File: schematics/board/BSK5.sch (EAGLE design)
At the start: 26 parts

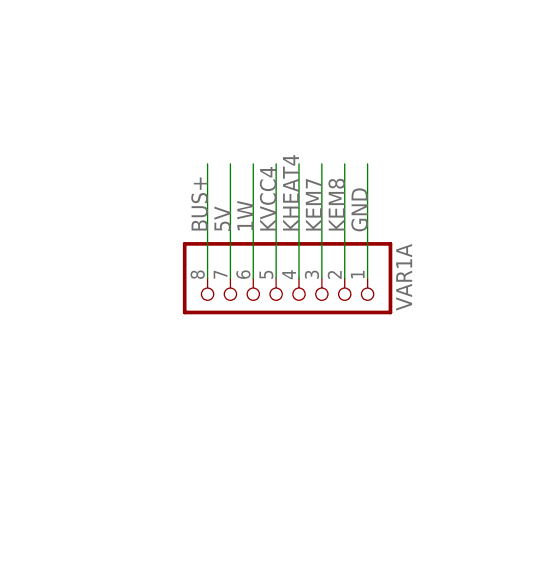
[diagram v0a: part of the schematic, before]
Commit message: Подписаны разъемы на платах
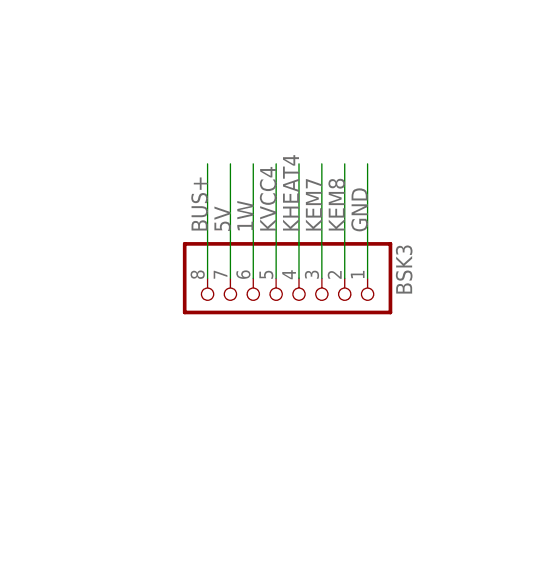
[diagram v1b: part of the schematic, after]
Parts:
- renumbered VAR1A to BSK3
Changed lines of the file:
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@@
 <part name="U$11" library="CanCubeSat" deviceset="KCONNECT" device=""/>
 <part name="U$12" library="CanCubeSat" deviceset="KCONNECT" device=""/>
-<part name="VAR1A" library="pinheadCS" deviceset="PINHD-1X8" device=""/>
+<part name="BSK3" library="pinheadCS" deviceset="PINHD-1X8" device=""/>
 <part name="LED2" library="led" library_urn="urn:adsk.eagle:library:259" deviceset="LED" device="CHIPLED_0603" package3d_urn="urn:adsk.eagle:package:15822/2"/>
 <part name="R81" library="resistor" library_urn="urn:adsk.eagle:library:348" deviceset="R-US_" device="R0603" package3d_urn="urn:adsk.eagle:package:23555/3" value="2k"/>
@@
 <attribute name="NAME" x="140.462" y="102.362" size="1.27" layer="95"/>
 </instance>
-<instance part="VAR1A" gate="A" x="154.94" y="175.26" smashed="yes" rot="R270">
+<instance part="BSK3" gate="A" x="154.94" y="175.26" smashed="yes" rot="R270">
 <attribute name="NAME" x="168.275" y="181.61" size="1.778" layer="95" rot="R270"/>
 <attribute name="VALUE" x="142.24" y="181.61" size="1.778" layer="96" rot="R270"/>
@@
 <wire x1="165.1" y1="177.8" x2="165.1" y2="190.5" width="0.1524" layer="91"/>
 <label x="165.1" y="182.88" size="1.778" layer="95" rot="R90"/>
-<pinref part="VAR1A" gate="A" pin="1"/>
+<pinref part="BSK3" gate="A" pin="1"/>
 </segment>
 </net>
@@
 <wire x1="149.86" y1="177.8" x2="149.86" y2="190.5" width="0.1524" layer="91"/>
 <label x="149.86" y="182.88" size="1.778" layer="95" rot="R90"/>
-<pinref part="VAR1A" gate="A" pin="7"/>
+<pinref part="BSK3" gate="A" pin="7"/>
 </segment>
 <segment>
@@
 <wire x1="152.4" y1="177.8" x2="152.4" y2="190.5" width="0.1524" layer="91"/>
 <label x="152.4" y="182.88" size="1.778" layer="95" rot="R90"/>
-<pinref part="VAR1A" gate="A" pin="6"/>
+<pinref part="BSK3" gate="A" pin="6"/>
 </segment>
 </net>
@@
 <wire x1="147.32" y1="177.8" x2="147.32" y2="190.5" width="0.1524" layer="91"/>
 <label x="147.32" y="182.88" size="1.778" layer="95" rot="R90"/>
-<pinref part="VAR1A" gate="A" pin="8"/>
+<pinref part="BSK3" gate="A" pin="8"/>
 </segment>
 <segment>
@@
 <wire x1="160.02" y1="177.8" x2="160.02" y2="190.5" width="0.1524" layer="91"/>
 <label x="160.02" y="182.88" size="1.778" layer="95" rot="R90"/>
-<pinref part="VAR1A" gate="A" pin="3"/>
+<pinref part="BSK3" gate="A" pin="3"/>
 </segment>
 <segment>
@@
 <wire x1="162.56" y1="177.8" x2="162.56" y2="190.5" width="0.1524" layer="91"/>
 <label x="162.56" y="182.88" size="1.778" layer="95" rot="R90"/>
-<pinref part="VAR1A" gate="A" pin="2"/>
+<pinref part="BSK3" gate="A" pin="2"/>
 </segment>
 <segment>
@@
 <wire x1="157.48" y1="177.8" x2="157.48" y2="190.5" width="0.1524" layer="91"/>
 <label x="157.48" y="182.88" size="1.778" layer="95" rot="R90"/>
-<pinref part="VAR1A" gate="A" pin="4"/>
+<pinref part="BSK3" gate="A" pin="4"/>
 </segment>
 <segment>
@@
 <wire x1="154.94" y1="177.8" x2="154.94" y2="190.5" width="0.1524" layer="91"/>
 <label x="154.94" y="182.88" size="1.778" layer="95" rot="R90"/>
-<pinref part="VAR1A" gate="A" pin="5"/>
-</segment>
-<segment>
+<pinref part="BSK3" gate="A" pin="5"/>
+</segment>
+<segment>

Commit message: Платы подготовлены для Резонита
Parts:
- removed U$14: FS8205A, CanCubeSat:FS8205A
- added FS8205A: FS8205A+, CanCubeSat:FS8205A+
- renumbered U$5 to DS18B20, U$8 to L293DD
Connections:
- removed net HEAT: DS18B20.HEAT, L293DD.HEAT, U$14.HEAT
- net BUS-: now also FS8205A.S1; no longer U$14.S1
- net GND: now also DS18B20.HEAT, FS8205A.HEAT, FS8205A.S2, L293DD.HEAT; no longer U$14.S2
- net N$8: now also FS8205A.G1; no longer U$14.G1
- net N$9: now also FS8205A.G2; no longer U$14.G2
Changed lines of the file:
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@@
 <?xml version="1.0" encoding="utf-8"?>
 <!DOCTYPE eagle SYSTEM "eagle.dtd">
-<eagle version="9.6.0">
+<eagle version="9.4.2">
 <drawing>
 <settings>
@@
 </classes>
 <parts>
-<part name="U$5" library="CanCubeSat" deviceset="DS18B20Z" device="" value="DS18B20Z"/>
+<part name="DS18B20" library="CanCubeSat" deviceset="DS18B20Z" device="" value="DS18B20Z"/>
 <part name="U$6" library="CanCubeSat" deviceset="EM_HEAT" device=""/>
 <part name="U$7" library="CanCubeSat" deviceset="EM_HEAT" device=""/>
-<part name="U$8" library="CanCubeSat" deviceset="L293DD" device=""/>
-<part name="U$14" library="CanCubeSat" deviceset="FS8205A" device=""/>
+<part name="L293DD" library="CanCubeSat" deviceset="L293DD" device=""/>
+<part name="FS8205A" library="CanCubeSat" deviceset="FS8205A+" device=""/>
 <part name="R10" library="resistor" library_urn="urn:adsk.eagle:library:348" deviceset="R-US_" device="R0603" package3d_urn="urn:adsk.eagle:package:23555/3" value="10k"/>
 <part name="R11" library="resistor" library_urn="urn:adsk.eagle:library:348" deviceset="R-US_" device="R0603" package3d_urn="urn:adsk.eagle:package:23555/3" value="10k"/>
@@
 </plain>
 <instances>
-<instance part="U$5" gate="G$1" x="157.48" y="231.14" smashed="yes"/>
+<instance part="DS18B20" gate="G$1" x="157.48" y="231.14" smashed="yes"/>
 <instance part="U$6" gate="G$1" x="58.42" y="139.7" smashed="yes" rot="R90"/>
 <instance part="U$7" gate="G$1" x="73.66" y="139.7" smashed="yes" rot="R270"/>
-<instance part="U$8" gate="G$1" x="66.04" y="111.76" smashed="yes" rot="R270"/>
-<instance part="U$14" gate="G$1" x="73.66" y="200.66" smashed="yes"/>
+<instance part="L293DD" gate="G$1" x="66.04" y="111.76" smashed="yes" rot="R270"/>
+<instance part="FS8205A" gate="G$1" x="73.66" y="200.66" smashed="yes"/>
 <instance part="R10" gate="G$1" x="68.58" y="218.44" smashed="yes" rot="R270">
 <attribute name="NAME" x="70.0786" y="222.25" size="1.778" layer="95" rot="R270"/>
@@
 </segment>
 <segment>
-<pinref part="U$5" gate="G$1" pin="GND"/>
+<pinref part="DS18B20" gate="G$1" pin="GND"/>
 <wire x1="167.64" y1="228.6" x2="175.26" y2="228.6" width="0.1524" layer="91"/>
 <label x="168.656" y="228.6" size="1.778" layer="95"/>
 </segment>
 <segment>
-<pinref part="U$8" gate="G$1" pin="GND"/>
+<pinref part="L293DD" gate="G$1" pin="GND"/>
 <wire x1="53.34" y1="114.3" x2="46.736" y2="114.3" width="0.1524" layer="91"/>
 <label x="47.244" y="114.3" size="1.778" layer="95"/>
 </segment>
 <segment>
-<pinref part="U$14" gate="G$1" pin="S2"/>
+<pinref part="FS8205A" gate="G$1" pin="S2"/>
 <wire x1="86.36" y1="200.66" x2="96.52" y2="200.66" width="0.1524" layer="91"/>
 <label x="91.44" y="200.66" size="1.778" layer="95"/>
@@
 <pinref part="BSK3" gate="A" pin="1"/>
 </segment>
+<segment>
+<pinref part="L293DD" gate="G$1" pin="HEAT"/>
+<wire x1="55.88" y1="109.22" x2="30.48" y2="109.22" width="0.1524" layer="91"/>
+<wire x1="30.48" y1="109.22" x2="30.48" y2="167.64" width="0.1524" layer="91"/>
+<wire x1="30.48" y1="167.64" x2="73.66" y2="167.64" width="0.1524" layer="91"/>
+<pinref part="FS8205A" gate="G$1" pin="HEAT"/>
+<wire x1="73.66" y1="167.64" x2="73.66" y2="193.04" width="0.1524" layer="91"/>
+<pinref part="DS18B20" gate="G$1" pin="HEAT"/>
+<wire x1="165.1" y1="233.68" x2="165.1" y2="241.3" width="0.1524" layer="91"/>
+<wire x1="165.1" y1="241.3" x2="106.68" y2="241.3" width="0.1524" layer="91"/>
+<wire x1="106.68" y1="241.3" x2="106.68" y2="167.64" width="0.1524" layer="91"/>
+<wire x1="106.68" y1="167.64" x2="73.66" y2="167.64" width="0.1524" layer="91"/>
+<junction x="73.66" y="167.64"/>
+<label x="66.04" y="167.64" size="1.778" layer="95"/>
+</segment>
 </net>
 <net name="5V" class="0">
 <segment>
-<pinref part="U$8" gate="G$1" pin="EN1"/>
+<pinref part="L293DD" gate="G$1" pin="EN1"/>
 <wire x1="53.34" y1="121.92" x2="48.26" y2="121.92" width="0.1524" layer="91"/>
 <label x="49.784" y="121.92" size="1.778" layer="95"/>
 </segment>
 <segment>
-<pinref part="U$8" gate="G$1" pin="VS"/>
+<pinref part="L293DD" gate="G$1" pin="VS"/>
 <wire x1="53.34" y1="99.06" x2="48.26" y2="99.06" width="0.1524" layer="91"/>
 <label x="49.53" y="99.06" size="1.778" layer="95"/>
 </segment>
 <segment>
-<pinref part="U$8" gate="G$1" pin="EN2"/>
+<pinref part="L293DD" gate="G$1" pin="EN2"/>
 <wire x1="78.74" y1="99.06" x2="83.82" y2="99.06" width="0.1524" layer="91"/>
 <label x="80.01" y="99.06" size="1.778" layer="95"/>
 </segment>
 <segment>
-<pinref part="U$8" gate="G$1" pin="VSS"/>
+<pinref part="L293DD" gate="G$1" pin="VSS"/>
 <wire x1="78.74" y1="121.92" x2="83.82" y2="121.92" width="0.1524" layer="91"/>
 <label x="79.756" y="121.92" size="1.778" layer="95"/>
@@
 </segment>
 <segment>
-<pinref part="U$5" gate="G$1" pin="VDD"/>
+<pinref part="DS18B20" gate="G$1" pin="VDD"/>
 <wire x1="144.78" y1="231.14" x2="137.16" y2="231.14" width="0.1524" layer="91"/>
 <label x="139.7" y="231.14" size="1.778" layer="95"/>
@@
 <net name="1W" class="0">
 <segment>
-<pinref part="U$5" gate="G$1" pin="DQ"/>
+<pinref part="DS18B20" gate="G$1" pin="DQ"/>
 <wire x1="144.78" y1="228.6" x2="137.16" y2="228.6" width="0.1524" layer="91"/>
 <label x="139.7" y="228.6" size="1.778" layer="95"/>
@@
 <wire x1="48.26" y1="137.16" x2="40.64" y2="137.16" width="0.1524" layer="91"/>
 <wire x1="40.64" y1="137.16" x2="40.64" y2="116.84" width="0.1524" layer="91"/>
-<pinref part="U$8" gate="G$1" pin="OUT1"/>
+<pinref part="L293DD" gate="G$1" pin="OUT1"/>
 <wire x1="40.64" y1="116.84" x2="53.34" y2="116.84" width="0.1524" layer="91"/>
 <pinref part="LED2" gate="G$1" pin="A"/>
@@
 <segment>
 <wire x1="35.56" y1="154.94" x2="35.56" y2="104.14" width="0.1524" layer="91"/>
-<pinref part="U$8" gate="G$1" pin="OUT2"/>
+<pinref part="L293DD" gate="G$1" pin="OUT2"/>
 <wire x1="35.56" y1="104.14" x2="53.34" y2="104.14" width="0.1524" layer="91"/>
 <wire x1="35.56" y1="154.94" x2="40.64" y2="154.94" width="0.1524" layer="91"/>
@@
 <segment>
 <wire x1="96.52" y1="154.94" x2="96.52" y2="116.84" width="0.1524" layer="91"/>
-<pinref part="U$8" gate="G$1" pin="OUT4"/>
+<pinref part="L293DD" gate="G$1" pin="OUT4"/>
 <wire x1="96.52" y1="116.84" x2="78.74" y2="116.84" width="0.1524" layer="91"/>
 <pinref part="U$7" gate="G$1" pin="5V"/>
@@
 <net name="BUS-" class="0">
 <segment>
-<pinref part="U$14" gate="G$1" pin="S1"/>
+<pinref part="FS8205A" gate="G$1" pin="S1"/>
 <wire x1="53.34" y1="200.66" x2="60.96" y2="200.66" width="0.1524" layer="91"/>
 <pinref part="R20" gate="G$1" pin="2"/>
@@
 <net name="N$8" class="0">
 <segment>
-<pinref part="U$14" gate="G$1" pin="G1"/>
+<pinref part="FS8205A" gate="G$1" pin="G1"/>
 <pinref part="R10" gate="G$1" pin="2"/>
 <wire x1="68.58" y1="213.36" x2="68.58" y2="210.82" width="0.1524" layer="91"/>
@@
 <pinref part="R11" gate="G$1" pin="2"/>
 <wire x1="78.74" y1="213.36" x2="78.74" y2="210.82" width="0.1524" layer="91"/>
-<pinref part="U$14" gate="G$1" pin="G2"/>
+<pinref part="FS8205A" gate="G$1" pin="G2"/>
 </segment>
 </net>
@@
 </segment>
 <segment>
-<pinref part="U$8" gate="G$1" pin="IN1"/>
+<pinref part="L293DD" gate="G$1" pin="IN1"/>
 <wire x1="53.34" y1="119.38" x2="45.72" y2="119.38" width="0.1524" layer="91"/>
 <label x="46.482" y="119.38" size="1.778" layer="95"/>
@@
 </segment>
 <segment>
-<pinref part="U$8" gate="G$1" pin="IN2"/>
+<pinref part="L293DD" gate="G$1" pin="IN2"/>
 <wire x1="53.34" y1="101.6" x2="45.72" y2="101.6" width="0.1524" layer="91"/>
 <label x="46.99" y="101.6" size="1.778" layer="95"/>
@@
 </segment>
 <segment>
-<pinref part="U$8" gate="G$1" pin="IN4"/>
+<pinref part="L293DD" gate="G$1" pin="IN4"/>
 <wire x1="78.74" y1="119.38" x2="88.9" y2="119.38" width="0.1524" layer="91"/>
 <label x="79.502" y="119.38" size="1.778" layer="95"/>
@@
 </segment>
 </net>
-<net name="HEAT" class="0">
-<segment>
-<pinref part="U$8" gate="G$1" pin="HEAT"/>
-<wire x1="55.88" y1="109.22" x2="30.48" y2="109.22" width="0.1524" layer="91"/>
-<wire x1="30.48" y1="109.22" x2="30.48" y2="167.64" width="0.1524" layer="91"/>
-<wire x1="30.48" y1="167.64" x2="73.66" y2="167.64" width="0.1524" layer="91"/>
-<pinref part="U$14" gate="G$1" pin="HEAT"/>
-<wire x1="73.66" y1="167.64" x2="73.66" y2="193.04" width="0.1524" layer="91"/>
-<pinref part="U$5" gate="G$1" pin="HEAT"/>
-<wire x1="165.1" y1="233.68" x2="165.1" y2="241.3" width="0.1524" layer="91"/>
-<wire x1="165.1" y1="241.3" x2="106.68" y2="241.3" width="0.1524" layer="91"/>
-<wire x1="106.68" y1="241.3" x2="106.68" y2="167.64" width="0.1524" layer="91"/>
-<wire x1="106.68" y1="167.64" x2="73.66" y2="167.64" width="0.1524" layer="91"/>
-<junction x="73.66" y="167.64"/>
-<label x="66.04" y="167.64" size="1.778" layer="95"/>
-</segment>
-</net>

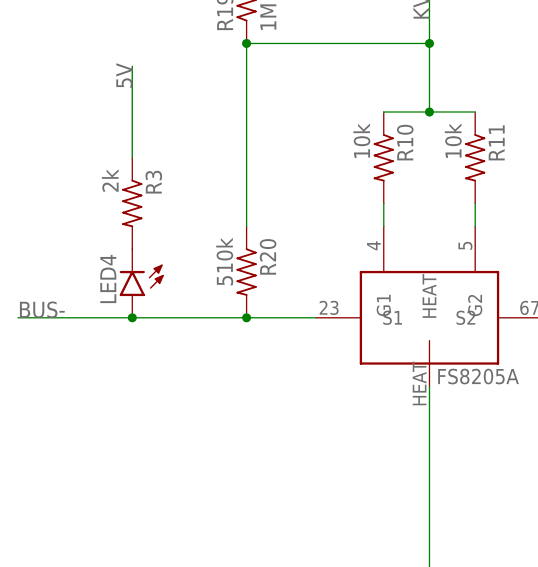
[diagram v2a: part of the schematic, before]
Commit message: Исправлены RADIO и диоды
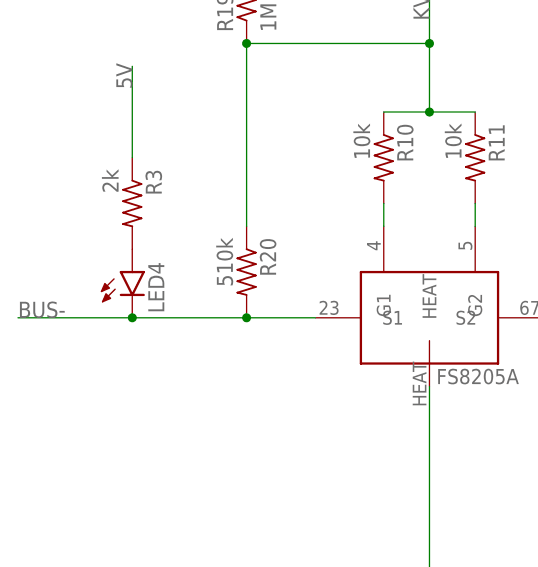
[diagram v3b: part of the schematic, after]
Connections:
- net BUS-: now also LED4.C; no longer LED4.A
- net N$29: now also LED4.A; no longer LED4.C
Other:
- moved on the sheet: LED4
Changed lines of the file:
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@@
 <part name="R2" library="resistor" library_urn="urn:adsk.eagle:library:348" deviceset="R-US_" device="R0603" package3d_urn="urn:adsk.eagle:package:23555/3" value="2k"/>
 <part name="LED3" library="led" library_urn="urn:adsk.eagle:library:259" deviceset="LED" device="CHIPLED_0603" package3d_urn="urn:adsk.eagle:package:15822/2"/>
+<part name="R3" library="resistor" library_urn="urn:adsk.eagle:library:348" deviceset="R-US_" device="R0603" package3d_urn="urn:adsk.eagle:package:23555/3" value="2k"/>
 <part name="LED4" library="led" library_urn="urn:adsk.eagle:library:259" deviceset="LED" device="CHIPLED_0603" package3d_urn="urn:adsk.eagle:package:15822/2"/>
-<part name="R3" library="resistor" library_urn="urn:adsk.eagle:library:348" deviceset="R-US_" device="R0603" package3d_urn="urn:adsk.eagle:package:23555/3" value="2k"/>
 </parts>
 <sheets>
@@
 <attribute name="VALUE" x="89.535" y="147.828" size="1.778" layer="96" rot="R90"/>
 </instance>
-<instance part="LED4" gate="G$1" x="40.64" y="203.2" smashed="yes" rot="R180">
-<attribute name="NAME" x="37.084" y="207.772" size="1.778" layer="95" rot="R270"/>
-<attribute name="VALUE" x="34.925" y="207.772" size="1.778" layer="96" rot="R270"/>
-</instance>
 <instance part="R3" gate="G$1" x="40.64" y="213.36" smashed="yes" rot="R270">
 <attribute name="NAME" x="42.1386" y="217.17" size="1.778" layer="95" rot="R270"/>
 <attribute name="VALUE" x="37.338" y="217.17" size="1.778" layer="96" rot="R270"/>
+</instance>
+<instance part="LED4" gate="G$1" x="40.64" y="205.74" smashed="yes">
+<attribute name="NAME" x="44.196" y="201.168" size="1.778" layer="95" rot="R90"/>
+<attribute name="VALUE" x="46.355" y="201.168" size="1.778" layer="96" rot="R90"/>
 </instance>
 </instances>
@@
 <wire x1="53.34" y1="200.66" x2="60.96" y2="200.66" width="0.1524" layer="91"/>
 <pinref part="R20" gate="G$1" pin="2"/>
-<wire x1="53.34" y1="200.66" x2="40.64" y2="200.66" width="0.1524" layer="91"/>
 <junction x="53.34" y="200.66"/>
 <label x="27.94" y="200.66" size="1.778" layer="95"/>
-<pinref part="LED4" gate="G$1" pin="A"/>
+<wire x1="53.34" y1="200.66" x2="40.64" y2="200.66" width="0.1524" layer="91"/>
+<pinref part="LED4" gate="G$1" pin="C"/>
 <wire x1="40.64" y1="200.66" x2="27.94" y2="200.66" width="0.1524" layer="91"/>
 <junction x="40.64" y="200.66"/>
@@
 <net name="N$29" class="0">
 <segment>
-<pinref part="LED4" gate="G$1" pin="C"/>
+<pinref part="LED4" gate="G$1" pin="A"/>
 <pinref part="R3" gate="G$1" pin="2"/>
 </segment>

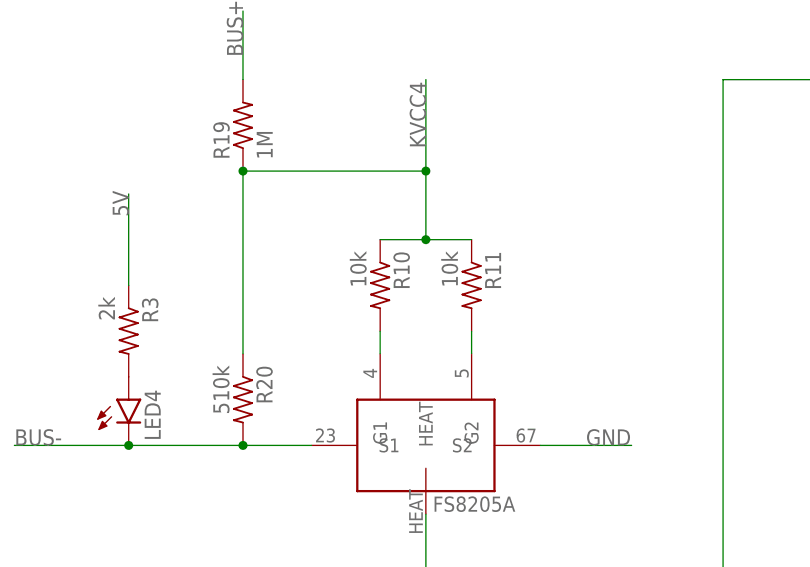
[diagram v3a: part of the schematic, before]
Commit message: Резисторы у FS8205A 100Ом
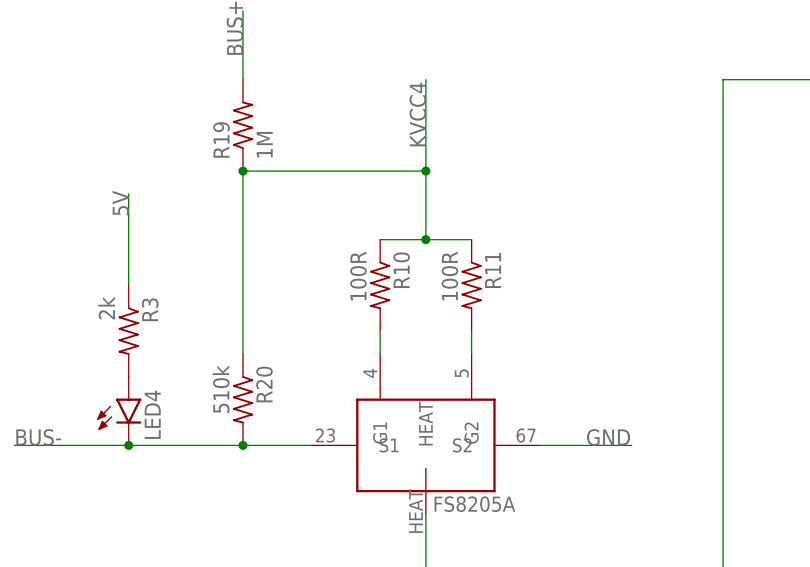
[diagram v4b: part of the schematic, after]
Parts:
- R10, R11: value 10k -> 100R
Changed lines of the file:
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@@
 <part name="L293DD" library="CanCubeSat" deviceset="L293DD" device=""/>
 <part name="FS8205A" library="CanCubeSat" deviceset="FS8205A+" device=""/>
-<part name="R10" library="resistor" library_urn="urn:adsk.eagle:library:348" deviceset="R-US_" device="R0603" package3d_urn="urn:adsk.eagle:package:23555/3" value="10k"/>
-<part name="R11" library="resistor" library_urn="urn:adsk.eagle:library:348" deviceset="R-US_" device="R0603" package3d_urn="urn:adsk.eagle:package:23555/3" value="10k"/>
+<part name="R10" library="resistor" library_urn="urn:adsk.eagle:library:348" deviceset="R-US_" device="R0603" package3d_urn="urn:adsk.eagle:package:23555/3" value="100R"/>
+<part name="R11" library="resistor" library_urn="urn:adsk.eagle:library:348" deviceset="R-US_" device="R0603" package3d_urn="urn:adsk.eagle:package:23555/3" value="100R"/>
 <part name="R19" library="resistor" library_urn="urn:adsk.eagle:library:348" deviceset="R-US_" device="R0603" package3d_urn="urn:adsk.eagle:package:23555/3" value="1M"/>
 <part name="R20" library="resistor" library_urn="urn:adsk.eagle:library:348" deviceset="R-US_" device="R0603" package3d_urn="urn:adsk.eagle:package:23555/3" value="510k"/>
